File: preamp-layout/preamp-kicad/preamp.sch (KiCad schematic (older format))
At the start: 13 parts, among them J1 AudioJack3, P1 Conn_WallPlug, SW1 SW_SPST, SW10 Rotary_Encoder_Switch, SW11 Rotary_Encoder_Switch, SW2 SW_Push_Open, SW3 SW_Push_Open, SW4 SW_Push_Open, SW5 SW_Push_Open, SW6 SW_Push_Open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

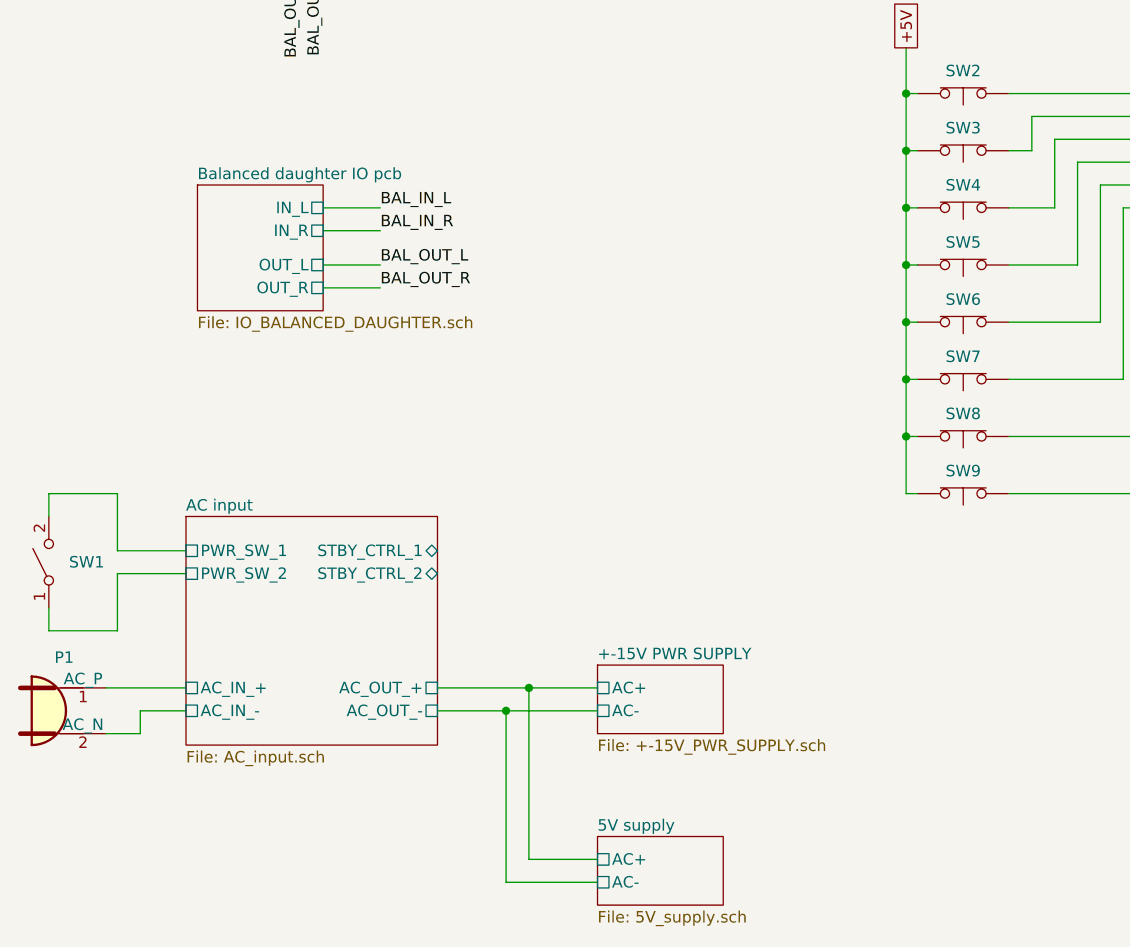
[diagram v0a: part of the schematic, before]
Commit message: Schematic Redesignation
Regenerated RefDes for all parts, updated BOM accordingly and perfomred check on values, RefDes present from schematic to BOM. Value changes, BOM filled in as a result.
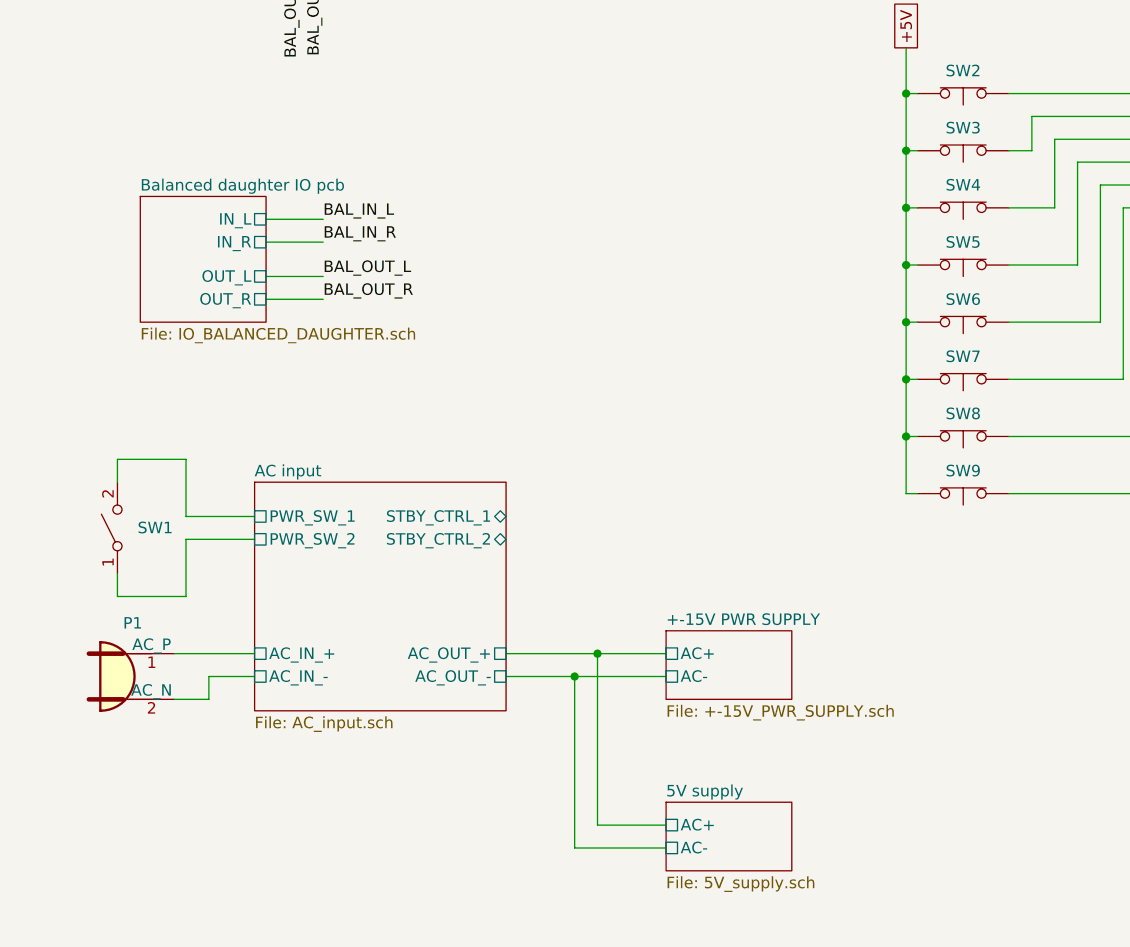
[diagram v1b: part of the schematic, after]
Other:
- moved on the sheet: P1, SW1
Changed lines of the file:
@@
 $EndDescr
 $Sheet
-S 1350 5800 1100 1000
+S 1650 5650 1100 1000
 U 5E26F6FE
 F0 "AC input" 50
 F1 "AC_input.sch" 50
-F2 "PWR_SW_1" U L 1350 5950 50
-F3 "PWR_SW_2" U L 1350 6050 50
-F4 "AC_OUT_+" U R 2450 6550 50
-F5 "AC_IN_-" U L 1350 6650 50
-F6 "AC_IN_+" U L 1350 6550 50
-F7 "AC_OUT_-" U R 2450 6650 50
-F8 "STBY_CTRL_2" B R 2450 6050 50
-F9 "STBY_CTRL_1" B R 2450 5950 50
-$EndSheet
-$Sheet
-S 3150 6450 550  300
+F2 "PWR_SW_1" U L 1650 5800 50
+F3 "PWR_SW_2" U L 1650 5900 50
+F4 "AC_OUT_+" U R 2750 6400 50
+F5 "AC_IN_-" U L 1650 6500 50
+F6 "AC_IN_+" U L 1650 6400 50
+F7 "AC_OUT_-" U R 2750 6500 50
+F8 "STBY_CTRL_2" B R 2750 5900 50
+F9 "STBY_CTRL_1" B R 2750 5800 50
+$EndSheet
+$Sheet
+S 3450 6300 550  300
 U 5E27B612
 F0 "+-15V PWR SUPPLY" 50
 F1 "+-15V_PWR_SUPPLY.sch" 50
-F2 "AC+" U L 3150 6550 50
-F3 "AC-" U L 3150 6650 50
-$EndSheet
-$Sheet
-S 3150 7200 550  300
+F2 "AC+" U L 3450 6400 50
+F3 "AC-" U L 3450 6500 50
+$EndSheet
+$Sheet
+S 3450 7050 550  300
 U 5E5EF2D4
 F0 "5V supply" 50
 F1 "5V_supply.sch" 50
-F2 "AC+" U L 3150 7300 50
-F3 "AC-" U L 3150 7400 50
+F2 "AC+" U L 3450 7150 50
+F3 "AC-" U L 3450 7250 50
 $EndSheet
 $Sheet
@@
 	8000 3500 8100 3600
 Wire Wire Line
-	2450 6550 2850 6550
-Wire Wire Line
-	2450 6650 2750 6650
-Wire Wire Line
-	2850 6550 2850 7300
-Wire Wire Line
-	2850 6550 3150 6550
-Wire Wire Line
-	2750 6650 2750 7400
-Wire Wire Line
-	2750 6650 3150 6650
+	2750 6400 3150 6400
+Wire Wire Line
+	2750 6500 3050 6500
+Wire Wire Line
+	3150 6400 3150 7150
+Wire Wire Line
+	3150 6400 3450 6400
+Wire Wire Line
+	3050 6500 3050 7250
+Wire Wire Line
+	3050 6500 3450 6500
 Wire Wire Line
 	1600 2850 2150 2850
@@
 L Switch:SW_SPST SW?
 U 1 1 5E2E8D21
-P 750 6000
+P 1050 5850
 AR Path="/5E26F6FE/5E2E8D21" Ref="SW?"  Part="1"
 AR Path="/5E2E8D21" Ref="SW1"  Part="1"
-F 0 "SW1" V 750 5912 50  0000 R CNN
-F 1 "SW_SPST" H 750 6144 50  0001 C CNN
-F 2 "" H 750 6000 50  0001 C CNN
-F 3 "~" H 750 6000 50  0001 C CNN
-	1    750  6000
+F 0 "SW1" V 1050 5762 50  0000 R CNN
+F 1 "SW_SPST" H 1050 5994 50  0001 C CNN
+F 2 "" H 1050 5850 50  0001 C CNN
+F 3 "~" H 1050 5850 50  0001 C CNN
+	1    1050 5850
 	0    -1   -1   0
 $EndComp
 Wire Wire Line
-	750  5800 750  5700
-Wire Wire Line
-	750  5700 1050 5700
-Wire Wire Line
-	1050 5700 1050 5950
-Wire Wire Line
-	1050 5950 1350 5950
-Wire Wire Line
-	750  6200 750  6300
-Wire Wire Line
-	750  6300 1050 6300
-Wire Wire Line
-	1050 6300 1050 6050
-Wire Wire Line
-	1050 6050 1350 6050
+	1050 5650 1050 5550
+Wire Wire Line
+	1050 5550 1350 5550
+Wire Wire Line
+	1350 5550 1350 5800
+Wire Wire Line
+	1350 5800 1650 5800
+Wire Wire Line
+	1050 6050 1050 6150
+Wire Wire Line
+	1050 6150 1350 6150
+Wire Wire Line
+	1350 6150 1350 5900
+Wire Wire Line
+	1350 5900 1650 5900
 $Comp
 L Connector:Conn_WallPlug P?
 U 1 1 5E300B43
-P 800 6650
+P 1100 6500
 AR Path="/5E26F6FE/5E300B43" Ref="P?"  Part="1"
 AR Path="/5E300B43" Ref="P1"  Part="1"
-F 0 "P1" H 817 6883 50  0000 C CNN
-F 1 "Conn_WallPlug" H 817 6884 50  0001 C CNN
-F 2 "" H 1200 6650 50  0001 C CNN
-F 3 "~" H 1200 6650 50  0001 C CNN
-	1    800  6650
+F 0 "P1" H 1117 6733 50  0000 C CNN
+F 1 "Conn_WallPlug" H 1117 6734 50  0001 C CNN
+F 2 "" H 1500 6500 50  0001 C CNN
+F 3 "~" H 1500 6500 50  0001 C CNN
+	1    1100 6500
 	1    0    0    -1
 $EndComp
 Wire Wire Line
-	1000 6550 1350 6550
-Wire Wire Line
-	1000 6750 1150 6750
-Wire Wire Line
-	1150 6750 1150 6650
-Wire Wire Line
-	1150 6650 1350 6650
+	1300 6400 1650 6400
+Wire Wire Line
+	1300 6600 1450 6600
+Wire Wire Line
+	1450 6600 1450 6500
+Wire Wire Line
+	1450 6500 1650 6500
 $Sheet
 S 8250 4500 550  300
@@
 BAL_IN_L
 Wire Wire Line
-	1950 4800 2200 4800
-Wire Wire Line
-	1950 4700 2200 4700
-Wire Wire Line
-	1950 4550 2200 4550
-Wire Wire Line
-	1950 4450 2200 4450
-Text Label 2200 4800 0    50   ~ 0
+	1700 4850 1950 4850
+Wire Wire Line
+	1700 4750 1950 4750
+Wire Wire Line
+	1700 4600 1950 4600
+Wire Wire Line
+	1700 4500 1950 4500
+Text Label 1950 4850 0    50   ~ 0
 BAL_OUT_R
-Text Label 2200 4700 0    50   ~ 0
+Text Label 1950 4750 0    50   ~ 0
 BAL_OUT_L
-Text Label 2200 4550 0    50   ~ 0
+Text Label 1950 4600 0    50   ~ 0
 BAL_IN_R
-Text Label 2200 4450 0    50   ~ 0
+Text Label 1950 4500 0    50   ~ 0
 BAL_IN_L
 $Sheet
-S 1400 4350 550  550
+S 1150 4400 550  550
 U 5E1A0CE1
 F0 "Balanced daughter IO pcb" 50
 F1 "IO_BALANCED_DAUGHTER.sch" 50
-F2 "OUT_R" U R 1950 4800 50
-F3 "OUT_L" U R 1950 4700 50
-F4 "IN_L" U R 1950 4450 50
-F5 "IN_R" U R 1950 4550 50
-$EndSheet
-Connection ~ 2750 6650
-Connection ~ 2850 6550
-Wire Wire Line
-	3150 7300 2850 7300
-Wire Wire Line
-	3150 7400 2750 7400
+F2 "OUT_R" U R 1700 4850 50
+F3 "OUT_L" U R 1700 4750 50
+F4 "IN_L" U R 1700 4500 50
+F5 "IN_R" U R 1700 4600 50
+$EndSheet
+Connection ~ 3050 6500
+Connection ~ 3150 6400
+Wire Wire Line
+	3450 7150 3150 7150
+Wire Wire Line
+	3450 7250 3050 7250
 Wire Bus Line
 	5200 1700 5200 3300

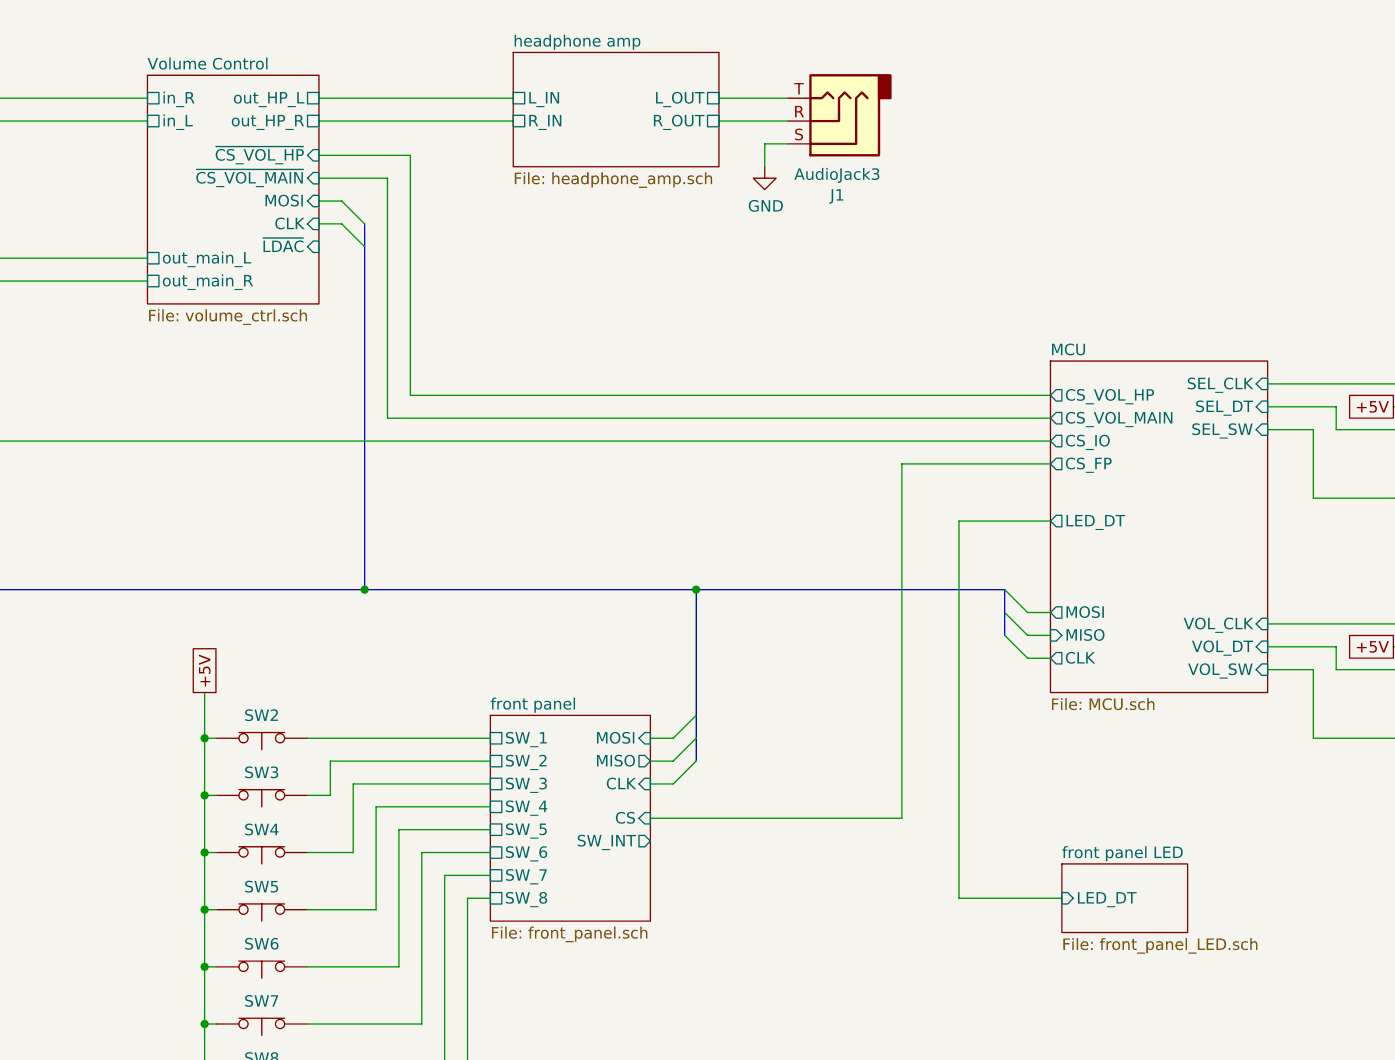
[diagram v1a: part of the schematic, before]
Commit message: Conn / Pin Updates
Updated cable headers, pin names, MCU conn layout. MCP4902 changeout for custom symbol.
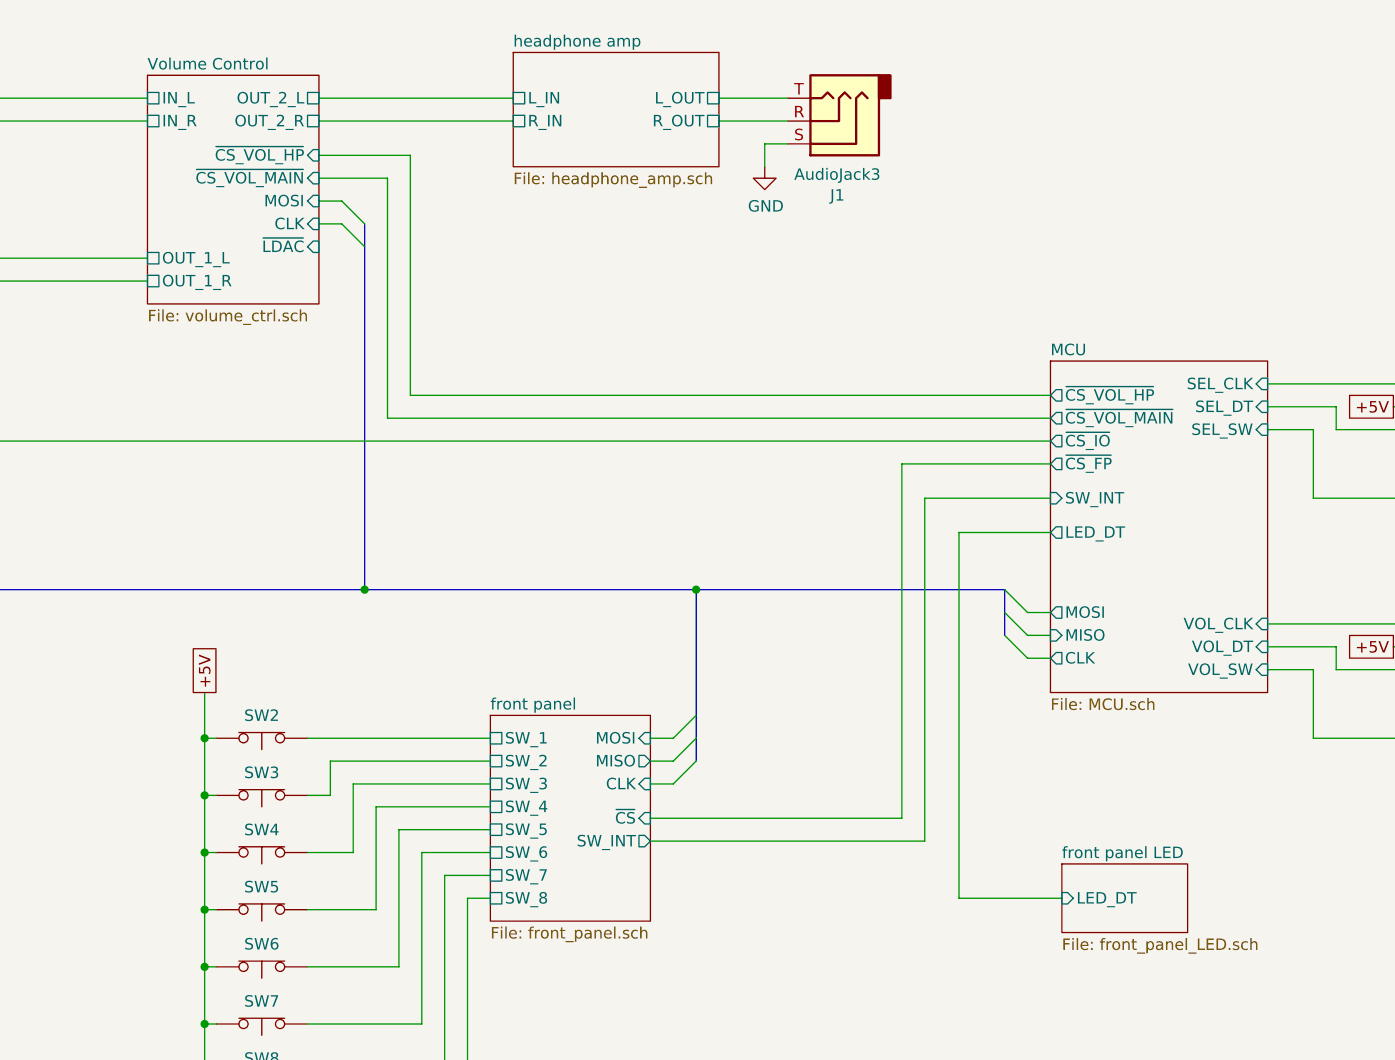
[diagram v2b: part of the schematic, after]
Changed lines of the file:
@@
 F3 "MOSI" I R 6450 3950 50
 F4 "CLK" I R 6450 4150 50
-F5 "CS" I R 6450 4300 50
-F6 "SW_INT" O R 6450 4400 50
-F7 "SW_1" U L 5750 3950 50
-F8 "SW_2" U L 5750 4050 50
-F9 "SW_3" U L 5750 4150 50
-F10 "SW_4" U L 5750 4250 50
-F11 "SW_5" U L 5750 4350 50
-F12 "SW_6" U L 5750 4450 50
-F13 "SW_7" U L 5750 4550 50
-F14 "SW_8" U L 5750 4650 50
+F5 "SW_INT" O R 6450 4400 50
+F6 "SW_1" U L 5750 3950 50
+F7 "SW_2" U L 5750 4050 50
+F8 "SW_3" U L 5750 4150 50
+F9 "SW_4" U L 5750 4250 50
+F10 "SW_5" U L 5750 4350 50
+F11 "SW_6" U L 5750 4450 50
+F12 "SW_7" U L 5750 4550 50
+F13 "SW_8" U L 5750 4650 50
+F14 "~CS" I R 6450 4300 50
 $EndSheet
 $Sheet
@@
 F3 "MOSI" O L 8200 3400 50
 F4 "CLK" O L 8200 3600 50
-F5 "CS_IO" O L 8200 2650 50
-F6 "SEL_CLK" I R 9150 2400 50
-F7 "SEL_DT" I R 9150 2500 50
-F8 "SEL_SW" I R 9150 2600 50
-F9 "VOL_CLK" I R 9150 3450 50
-F10 "VOL_DT" I R 9150 3550 50
-F11 "VOL_SW" I R 9150 3650 50
-F12 "CS_FP" O L 8200 2750 50
-F13 "LED_DT" O L 8200 3000 50
-F14 "CS_VOL_HP" O L 8200 2450 50
-F15 "CS_VOL_MAIN" O L 8200 2550 50
+F5 "SEL_CLK" I R 9150 2400 50
+F6 "SEL_DT" I R 9150 2500 50
+F7 "SEL_SW" I R 9150 2600 50
+F8 "VOL_CLK" I R 9150 3450 50
+F9 "VOL_DT" I R 9150 3550 50
+F10 "VOL_SW" I R 9150 3650 50
+F11 "LED_DT" O L 8200 3050 50
+F12 "SW_INT" I L 8200 2900 50
+F13 "~CS_FP" O L 8200 2750 50
+F14 "~CS_VOL_HP" O L 8200 2450 50
+F15 "~CS_VOL_MAIN" O L 8200 2550 50
+F16 "~CS_IO" O L 8200 2650 50
 $EndSheet
 $Sheet
@@
 $EndSheet
 Wire Wire Line
-	8200 3000 7800 3000
-Wire Wire Line
-	7800 3000 7800 4650
+	8200 3050 7800 3050
 Wire Wire Line
 	7800 4650 8250 4650
@@
 F0 "Volume Control" 50
 F1 "volume_ctrl.sch" 50
-F2 "in_R" U L 4250 1150 50
-F3 "in_L" U L 4250 1250 50
-F4 "out_main_L" U L 4250 1850 50
-F5 "out_main_R" U L 4250 1950 50
-F6 "out_HP_L" U R 5000 1150 50
-F7 "out_HP_R" U R 5000 1250 50
-F8 "~CS_VOL_HP" I R 5000 1400 50
-F9 "~CS_VOL_MAIN" I R 5000 1500 50
-F10 "~LDAC" I R 5000 1800 50
-F11 "MOSI" I R 5000 1600 50
-F12 "CLK" I R 5000 1700 50
+F2 "~CS_VOL_HP" I R 5000 1400 50
+F3 "~CS_VOL_MAIN" I R 5000 1500 50
+F4 "~LDAC" I R 5000 1800 50
+F5 "MOSI" I R 5000 1600 50
+F6 "CLK" I R 5000 1700 50
+F7 "OUT_1_L" U L 4250 1850 50
+F8 "OUT_1_R" U L 4250 1950 50
+F9 "OUT_2_L" U R 5000 1150 50
+F10 "OUT_2_R" U R 5000 1250 50
+F11 "IN_R" U L 4250 1250 50
+F12 "IN_L" U L 4250 1150 50
 $EndSheet
 $Comp
@@
 Wire Wire Line
 	3450 7250 3050 7250
+Wire Wire Line
+	7800 3050 7800 4650
+Wire Wire Line
+	6450 4400 7650 4400
+Wire Wire Line
+	7650 4400 7650 2900
+Wire Wire Line
+	7650 2900 8200 2900
 Wire Bus Line
 	5200 1700 5200 3300
